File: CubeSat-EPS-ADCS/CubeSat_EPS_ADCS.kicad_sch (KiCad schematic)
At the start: 14 parts, among them J1 Conn_01x02_Pin, J2 Conn_01x03_Pin, J3 Conn_01x08_Pin, J4 Screw_Terminal_01x02, J5 Screw_Terminal_01x02, J6 Screw_Terminal_01x02, J7 Screw_Terminal_01x02, J8 Screw_Terminal_01x02, U1 DRV8833 Module, U2 DRV8833 Module, U3 Buck_XL4015, U4 Buck_LM2596

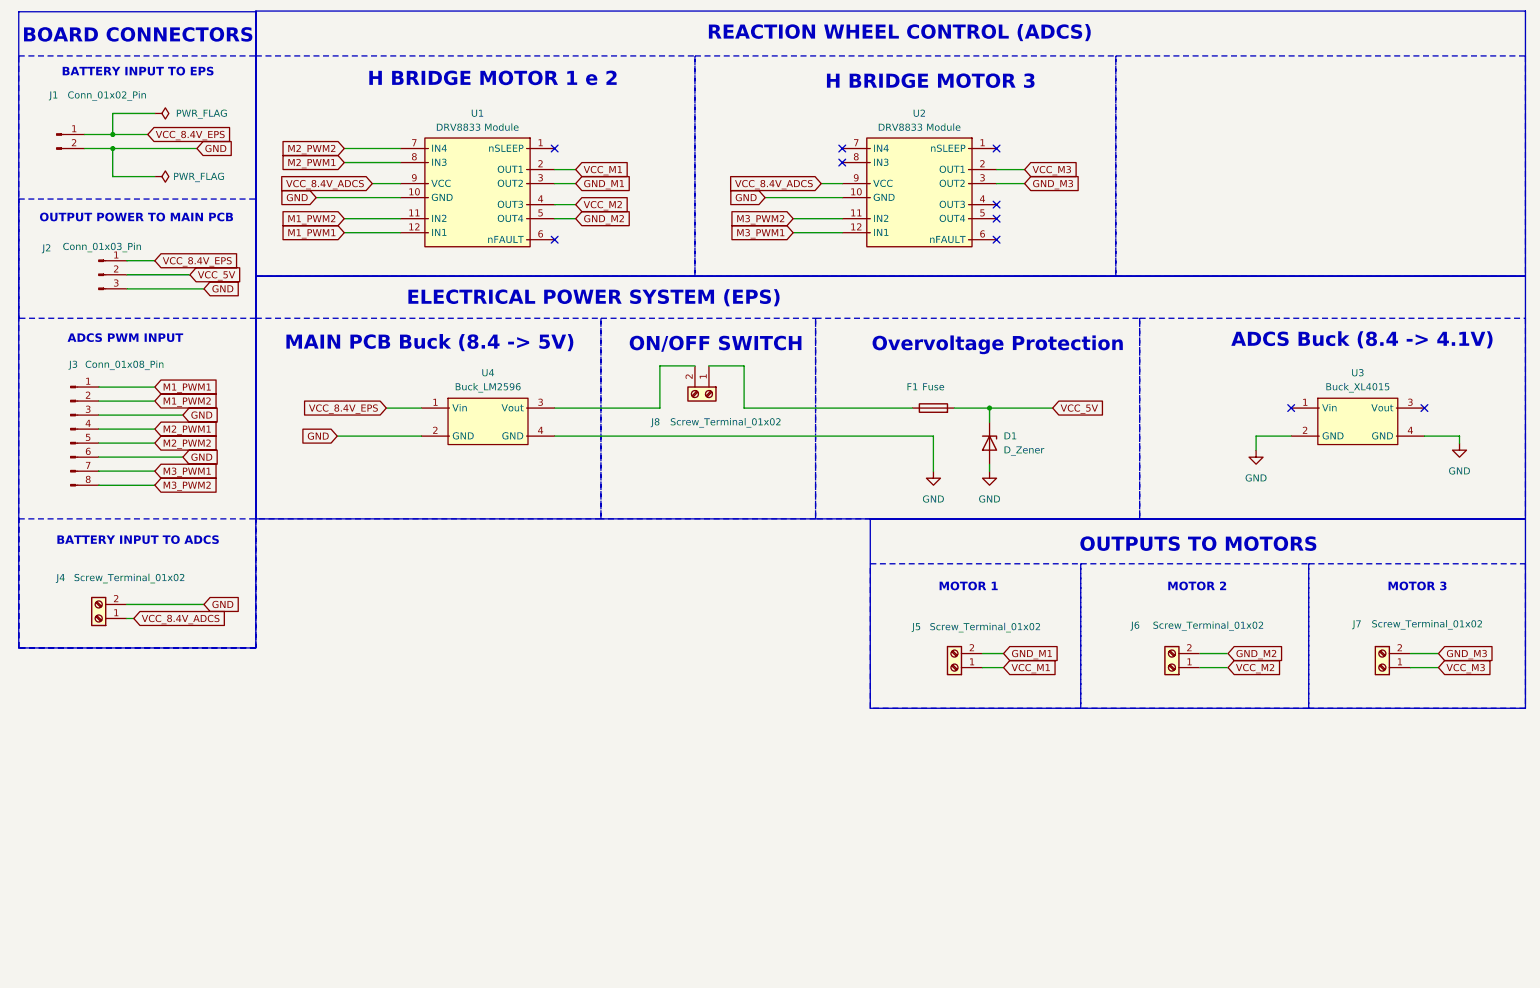
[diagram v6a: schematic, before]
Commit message: new Main and EPS PCBs, all previous problems corrected, final version
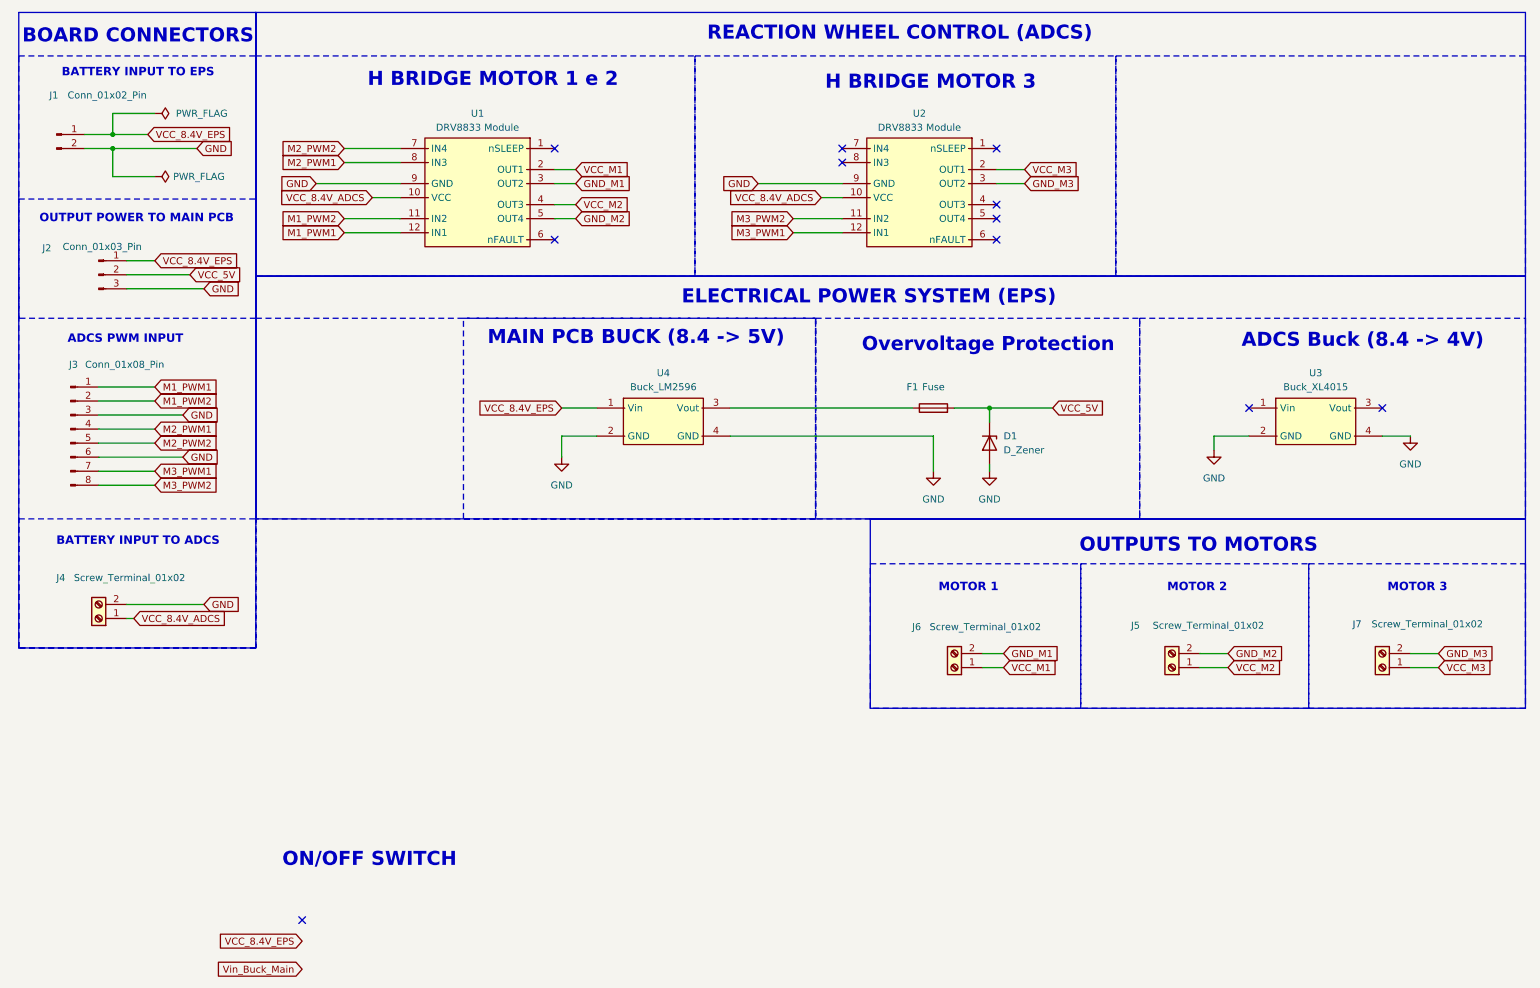
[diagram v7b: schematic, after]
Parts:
- removed J8: Screw_Terminal_01x02, TerminalBlock_Phoenix:TerminalBlock_Phoenix_MKDS-1,5-2_1x02_P5.00mm_Horizontal, symbol Connector:Screw_Terminal_01x02
- renumbered J6 to J5, J5 to J6
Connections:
- net GND: now also U1.9 (GND), U2.9 (GND); no longer U1.10 (GND), U2.10 (GND)
- net VCC_8.4V_ADCS: now also U1.10 (VCC), U2.10 (VCC); no longer U1.9 (VCC), U2.9 (VCC)
- net at F1.1: now also U4.3 (Vout)
- no-connect marks 10 -> 11
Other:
- note added: "ADCS Buck (8.4 -> 4V)"
- note added: "MAIN PCB BUCK (8.4 -> 5V)"
- note removed: "ADCS Buck (8.4 -> 4.1V)"
- note removed: "MAIN PCB Buck (8.4 -> 5V)"
- moved on the sheet: U3, U4
